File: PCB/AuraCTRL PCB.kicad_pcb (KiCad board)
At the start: 2 copper layers, 90 x 153.7 mm, 18 parts, among them SW1 RotaryEncoder_Switch, SW5 SW_Push, SW6 SW_Push, SW7 SW_Push, SW8 SW_Push, U1 XIAO-ESP32-C3-DIP

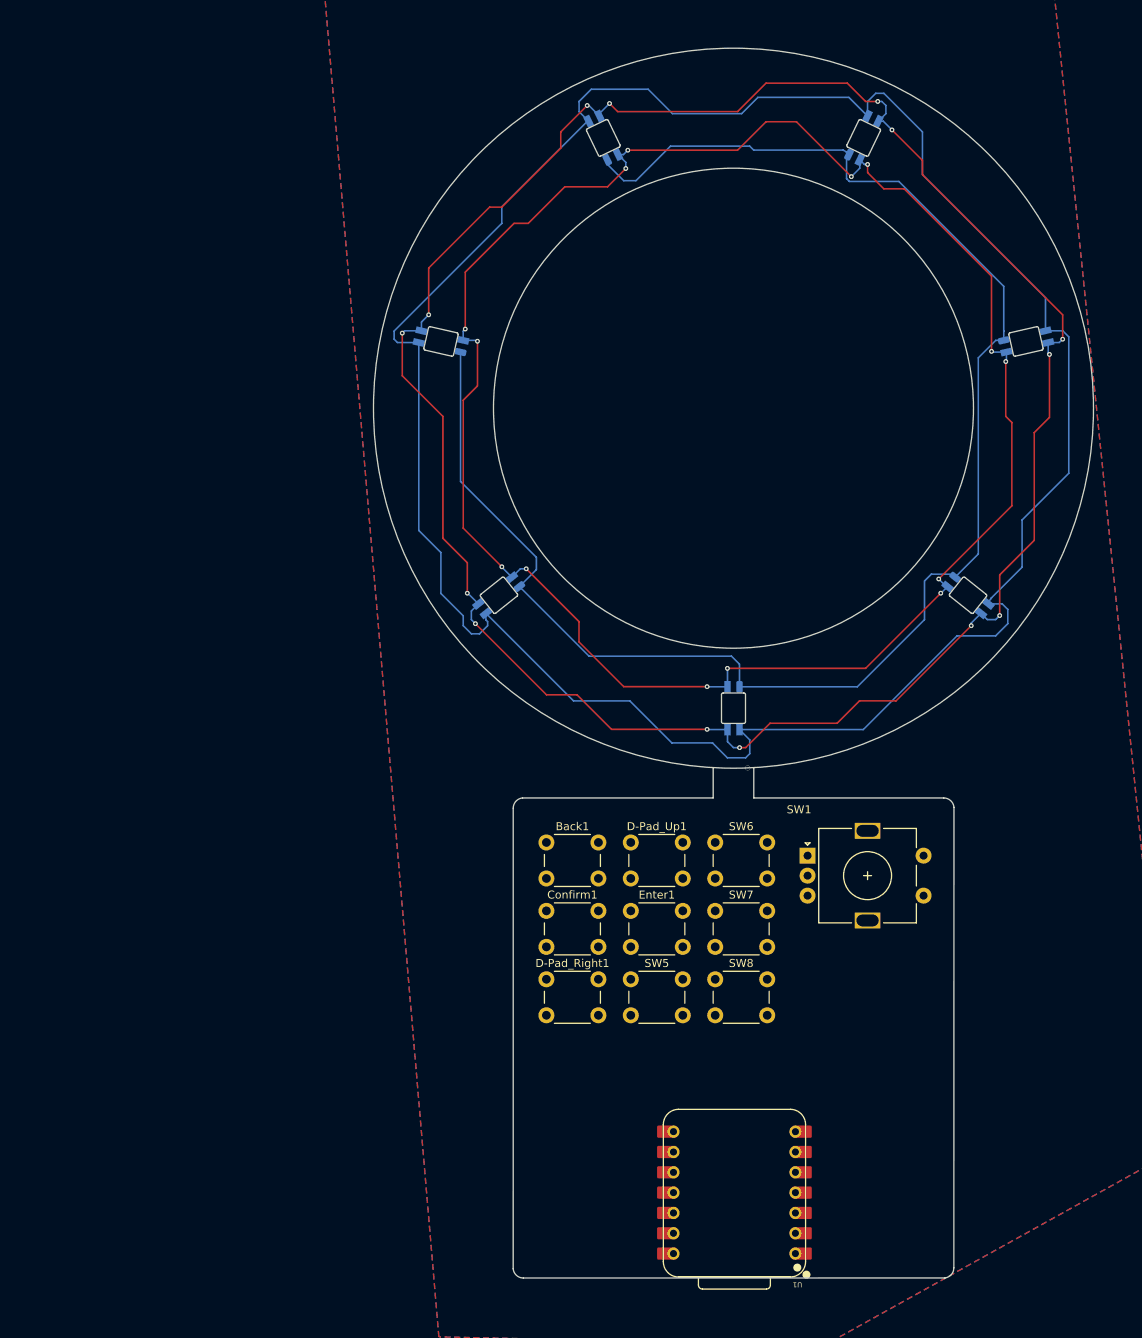
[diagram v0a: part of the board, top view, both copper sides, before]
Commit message: added the display, rewired neopixels, pcb outline
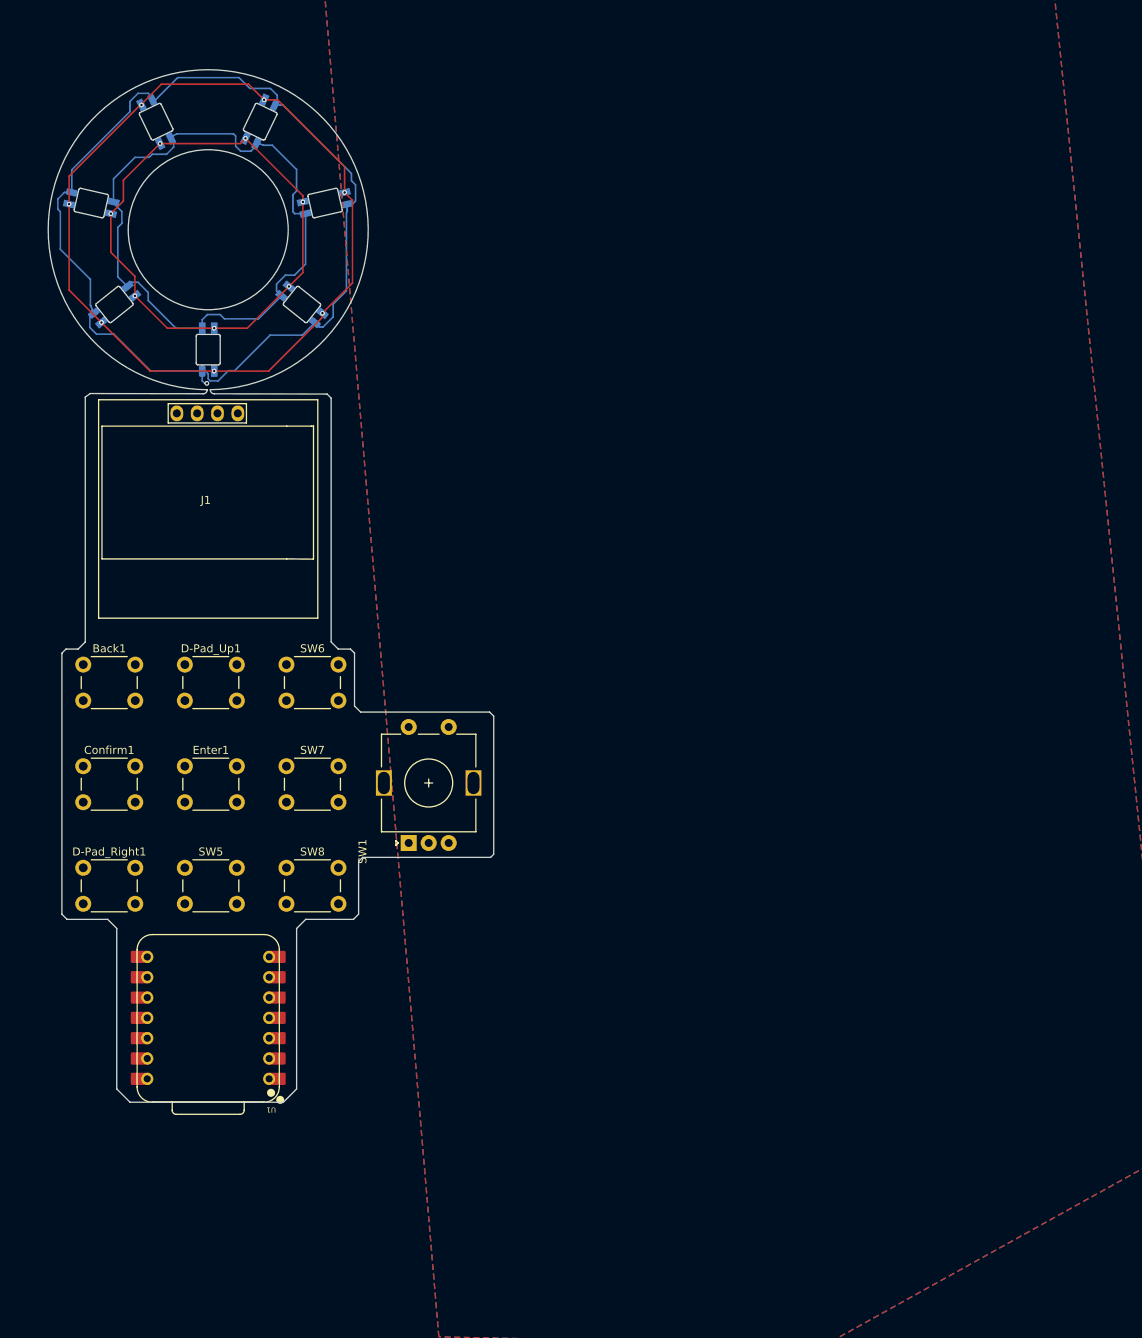
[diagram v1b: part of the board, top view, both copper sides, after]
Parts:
- removed the D1 at (115.8, 71.7)
- removed the D1 at (136.1, 46.2)
- removed the D1 at (152.4, 117.5)
- removed the D1 at (168.7, 46.2)
- removed the D1 at (123.1, 103.4)
- removed the D1 at (189.0, 71.7)
- removed the D1 at (181.7, 103.4)
- added D1: SK6812MINI, libs:SK6812-MINI-E, B.Cu at (72.1, 54.4)
- added D1: SK6812MINI, libs:SK6812-MINI-E, B.Cu at (86.7, 72.7)
- added D1: SK6812MINI, libs:SK6812-MINI-E, B.Cu at (80.2, 44.2)
- added D1: SK6812MINI, libs:SK6812-MINI-E, B.Cu at (75.0, 67.0)
- added D1: SK6812MINI, libs:SK6812-MINI-E, B.Cu at (98.5, 67.0)
- added D1: SK6812MINI, libs:SK6812-MINI-E, B.Cu at (93.2, 44.2)
- added D1: SK6812MINI, libs:SK6812-MINI-E, B.Cu at (101.4, 54.4)
- added J1: Conn_01x04, libs:128x64OLED, F.Cu at (86.4, 91.2)
- moved U1 69.3 mm to (86.6, 156.2)
- moved Back1 62.0 mm to (71.1, 112.0)
- moved Confirm1 60.7 mm to (71.1, 124.8)
- moved D-Pad_Up1 60.0 mm to (83.8, 112.0)
- moved D-Pad_Right1 59.5 mm to (71.1, 137.4)
- moved Enter1 58.6 mm to (83.8, 124.8)
- moved SW6 58.0 mm to (96.5, 112.0)
- moved SW5 57.5 mm to (83.8, 137.4)
- moved SW7 56.6 mm to (96.5, 124.8)
- moved SW8 55.4 mm to (96.5, 137.4)
- moved SW1 49.9 mm to (111.8, 134.3), turned to 90 degrees
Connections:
- U1 pad 12: unconnected-(U1-VCC_3V3-Pad12) -> 3v3
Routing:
- net Net-(D1-VSS): track 297.4 -> 89.4 mm
- net Net-(D1-DOUT): track 281.8 -> 79.1 mm, vias 14 -> 7
- net Net-(D1-VDD): track 244.5 -> 117.2 mm, vias 14 -> 7
- net Net-(D1-DIN): track 205.9 -> 129.4 mm, vias 0 -> 1
- net (no net): vias 1 -> 0
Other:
- board size 90 x 153.7 mm -> 55.7 x 129.1 mm
